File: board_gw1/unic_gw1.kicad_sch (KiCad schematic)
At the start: 109 parts, among them Q1 2N7002, Q10 2N7002, Q11 2N7002, Q12 2N7002, Q13 2N7002, Q14 2N7002, Q15 2N7002, Q16 2N7002, Q17 2N7002, Q18 2N7002, Q19 2N7002, Q2 2N7002, Q20 2N7002, Q21 2N7002, Q22 2N7002, Q23 2N7002, Q24 2N7002, Q25 2N7002, Q26 2N7002, Q27 2N7002, Q28 2N7002, Q29 2N7002, Q3 2N7002, Q30 2N7002, Q31 2N7002, Q32 2N7002, Q33 2N7002, Q34 2N7002, Q35 2N7002, Q36 2N7002, Q37 2N7002, Q38 2N7002, Q39 2N7002, Q4 2N7002, Q40 2N7002, Q5 2N7002, Q6 2N7002, Q7 2N7002, Q8 2N7002, Q9 2N7002, U1 GW1N-LV9QN88C6_I5_, U2 LM3480-3.3, U3 LM3480-5.0, U4 ESP-PSRAM32, U5 AT25SF081-XMHF-X, U6 AP62150Z6, X1 ASE-xxxMHz

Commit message: Added extra diodes to shunt ESD path.
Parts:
- added D21, D22, D23, D24, D25, D26, D27, D28, D29, D30: BAT54CV, Package_TO_SOT_SMD:SOT-666, symbol UNIC:BAT54CV
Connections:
- net +3V3: now also D21.3 (A), D21.3 (A), D21.6 (A), D21.6 (A), D22.3 (A), D22.3 (A), D22.6 (A), D22.6 (A), D23.3 (A), D23.3 (A), D23.6 (A), D23.6 (A), D24.3 (A), D24.3 (A), D24.6 (A), D24.6 (A), D25.3 (A), D25.3 (A), D25.6 (A), D25.6 (A), D26.3 (A), D26.3 (A), D26.6 (A), D26.6 (A), D27.3 (A), D27.3 (A), D27.6 (A), D27.6 (A), D28.3 (A), D28.3 (A), D28.6 (A), D28.6 (A), D29.3 (A), D29.3 (A), D29.6 (A), D29.6 (A), D30.3 (A), D30.3 (A), D30.6 (A), D30.6 (A)
- net PIN10_F: now also D23.2 (K)
- net PIN11_F: now also D23.4 (K)
- net PIN12_F: now also D23.5 (K)
- net PIN13_F: now also D24.1 (K)
- net PIN14_F: now also D24.2 (K)
- net PIN15_F: now also D24.4 (K)
- net PIN16_F: now also D24.5 (K)
- net PIN17_F: now also D25.1 (K)
- net PIN18_F: now also D25.2 (K)
- net PIN19_F: now also D25.4 (K)
- net PIN1_F: now also D21.1 (K)
- net PIN20_F: now also D25.5 (K)
- net PIN21_F: now also D26.1 (K)
- net PIN22_F: now also D26.2 (K)
- net PIN23_F: now also D26.4 (K)
- net PIN24_F: now also D26.5 (K)
- net PIN25_F: now also D27.1 (K)
- net PIN26_F: now also D27.2 (K)
- net PIN27_F: now also D27.4 (K)
- net PIN28_F: now also D27.5 (K)
- net PIN29_F: now also D28.1 (K)
- net PIN2_F: now also D21.2 (K)
- net PIN30_F: now also D28.2 (K)
- net PIN31_F: now also D28.4 (K)
- net PIN32_F: now also D28.5 (K)
- net PIN33_F: now also D29.1 (K)
- net PIN34_F: now also D29.2 (K)
- net PIN35_F: now also D29.4 (K)
- net PIN36_F: now also D29.5 (K)
- net PIN37_F: now also D30.1 (K)
- net PIN38_F: now also D30.2 (K)
- net PIN39_F: now also D30.4 (K)
- net PIN3_F: now also D21.4 (K)
- net PIN40_F: now also D30.5 (K)
- net PIN4_F: now also D21.5 (K)
- net PIN5_F: now also D22.1 (K)
- net PIN6_F: now also D22.2 (K)
- net PIN7_F: now also D22.4 (K)
- net PIN8_F: now also D22.5 (K)
- net PIN9_F: now also D23.1 (K)
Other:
- note added: "TODO: 3.3 needs to be a switcher! At 12V input power we can't sustain even 100mA I/O current. Static input current for an LS gate is 0.1mA. This gives us <10mA static output current. *THAT* We can sustain with an LDO See http://raven1.magix.net/Ti%20TTL%20DataBook%20vol1.pdf, page 20 https://ecelabs.njit.edu/fed101/resources/Motorola_Short_Version.pdf page 12 Detailed answer: https://electronics.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"
- note added: "There are dual- 7002 devices. https://assets.nexperia.com/documents/data-sheet/NX7002BKXB.pdf https://toshiba.semicon-storage.com/info/SSM6N7002BFE_datasheet_en_20140301.pdf?did=2282&prodName=SSM6N7002BFE https://www.diodes.com/assets/Datasheets/ds30639.pdf - has multiple sources All of these are cheaper than 2 single ones"
- moved on the sheet: C18, C20, C22, C23, D10A, D10B, D11A, D11B, D12A, D12B, D13A, D13B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

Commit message: GW1-based board is fully routed. Cleanup still needed!
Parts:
- removed D1, D10, D11, D12, D13, D14, D15, D16, D17, D18, D19, D2, D20, D3, D4, D5, D6, D7, D8, D9: BAT54SDW-7-F, UNIC:SOT65P210X110-6N, symbol UNIC:BAT54SDW-7-F
- removed J_EXT1: Conn_01x23_MountingPin, UNIC:Molex_502598-2393_2Rows-23Pins-1MP_P0.60mm_Horizontal, symbol Connector_Generic_MountingPin:Conn_01x23_MountingPin
- removed U3: LM3480-5.0, Package_TO_SOT_SMD:SOT-23, symbol Regulator_Linear:LM3480-5.0
- added D1, D11, D2, D3, D4, D5, D6, D7, D8, D9: BAT54DF, UNIC:SOT65P210X110-6N, symbol UNIC:BAT54DF
- added J_EXT1: Conn_01x27_MountingPin, UNIC:Molex_502598-2793_2Rows-23P~0.60mm_Horizontal, symbol Connector_Generic_MountingPin:Conn_01x27_MountingPin
- added R14: 4.99k, Resistor_SMD:R_0402_1005Metric_Pad0.72x0.64mm_HandSolder, symbol Device:R_Small_US
- added R15, R16: 10k, Resistor_SMD:R_0402_1005Metric_Pad0.72x0.64mm_HandSolder, symbol Device:R_Small_US
- added U3: AP2202K-ADJ, Package_TO_SOT_SMD:SOT-23-5, symbol Regulator_Linear:AP2204K-ADJ
- C3: value 0.1u -> 2.2u
- J_JTAG1: footprint Connector_PinHeader_1.27mm:PinHeader_2x06_P1.27mm_Vertical_SMD -> UNIC:PinHeader_2x06_P1.27mm_Vertical_SMD
- Q1, Q10, Q11, Q12, Q13, Q14, Q15, Q16, Q17, Q18, Q19, Q2, Q20, Q21, Q22, Q23, Q24, Q25, Q26, Q27, Q28, Q29, Q3, Q30, Q31, Q32, Q33, Q34, Q35, Q36, Q37, Q38, Q39, Q4, Q40, Q5, Q6, Q7, Q8, Q9: footprint Package_DFN_QFN:Diodes_DFN1006-3 -> UNIC:SOT-883
- R11, R3: value 1k -> 10k
- R12: value DNC -> 10k
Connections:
- net RECONIFG_N is gone; now on net RECONFIG_N: R7.2, U1.9 (IOL13B/RECONFIG_N)
- net SER_RXD is gone; now on net IO6B: J_JTAG1.1 (Pin_1)
- net SER_TXD is gone; now on net IO6A: J_JTAG1.2 (Pin_2)
- net +3V3: now also J_EXT1.25 (Pin_25), J_EXT1.26 (Pin_26), R16.1
- net +5V: now also J_EXT1.27 (Pin_27), R14.1, U3.5 (VOUT)
- net GND: now also D1.5, D1.5, D1.5, D1.5, D11.5, D11.5, D11.5, D11.5, D2.5, D2.5, D2.5, D2.5, D3.5, D3.5, D3.5, D3.5, D4.5, D4.5, D4.5, D4.5, D5.5, D5.5, D5.5, D5.5, D6.5, D6.5, D6.5, D6.5, D7.5, D7.5, D7.5, D7.5, D8.5, D8.5, D8.5, D8.5, D9.5, D9.5, D9.5, D9.5, J_EXT1.11 (Pin_11), J_EXT1.14 (Pin_14), J_EXT1.17 (Pin_17), J_EXT1.20 (Pin_20), J_EXT1.23 (Pin_23), J_EXT1.8 (Pin_8), J_EXT1.MP (MountPin), R15.2, U3.2 (GND)
- net IO1A: now also J_EXT1.7 (Pin_7)
- net IO1B: now also U1.38 (IOB31B), J_EXT1.9 (Pin_9); no longer U1.36 (IOB29B/GCLKC_4)
- net IO2A: now also U1.36 (IOB29B/GCLKC_4), J_EXT1.10 (Pin_10); no longer U1.35 (IOB29A/GCLKT_4)
- net IO2B: now also U1.35 (IOB29A/GCLKT_4), J_EXT1.12 (Pin_12); no longer U1.34 (IOB23B)
- net IO3A: now also U1.39 (IOB33A), J_EXT1.13 (Pin_13); no longer U1.33 (IOB23A)
- net IO3B: now also U1.40 (IOB33B), J_EXT1.15 (Pin_15); no longer U1.32 (IOB17B)
- net IO4A: now also J_EXT1.16 (Pin_16)
- net IO4B: now also U1.32 (IOB17B), J_EXT1.18 (Pin_18); no longer U1.30 (IOB13B)
- net IO5A: now also U1.41 (IOB41A), J_EXT1.19 (Pin_19); no longer U1.29 (IOB13A)
- net IO5B: now also U1.42 (IOB41B), J_EXT1.21 (Pin_21); no longer U1.28 (IOB11B)
- net IO6A: now also U1.33 (IOB23A), J_EXT1.22 (Pin_22); no longer U1.26 (IOB8B)
- net IO6B: now also U1.34 (IOB23B), J_EXT1.24 (Pin_24); no longer U1.25 (IOB8A)
- net JTAG_SEL_N: now also J_EXT1.1 (Pin_1), R16.2
- net JTAG_TCK: now also J_EXT1.6 (Pin_6)
- net JTAG_TDI: now also J_JTAG1.10 (Pin_10), J_EXT1.2 (Pin_2)
- net JTAG_TDO: now also J_EXT1.4 (Pin_4); no longer J_JTAG1.10 (Pin_10)
- net JTAG_TMS: now also J_EXT1.5 (Pin_5)
- net LCD_CS_N: now also U1.79 (IOT12B); no longer U1.54 (IOR15A/DIN/CLKHOLD_N)
- net LCD_RST_N: now also R2.2, R3.1, U1.87 (IOT6B/MODE1); no longer U1.53 (IOR15B/DOUT/WE_N)
- net LINE: now also D1.2, D1.2, D1.2, D1.2, D11.2, D11.2, D11.2, D11.2, D2.2, D2.2, D2.2, D2.2, D3.2, D3.2, D3.2, D3.2, D4.2, D4.2, D4.2, D4.2, D5.2, D5.2, D5.2, D5.2, D6.2, D6.2, D6.2, D6.2, D7.2, D7.2, D7.2, D7.2, D8.2, D8.2, D8.2, D8.2, D9.2, D9.2, D9.2, D9.2, U3.1 (VIN), U3.3 (EN)
- net PIN1: now also D1.1
- net PIN10: now also D3.3
- net PIN10_F: now also U1.69 (IOT42A); no longer U1.51 (IOR17B/GCLKC_3)
- net PIN11: now also Q19.3 (D), D5.1; no longer Q11.3 (D)
- net PIN11_F: now also D25.1 (K), Q19.2 (S), U1.73 (IOT39A); no longer D23.4 (K), Q11.2 (S), U1.63 (IOR5A/RPLL_T_IN)
- net PIN12: now also Q15.3 (D), D4.1; no longer Q12.3 (D)
- net PIN12_F: now also D24.1 (K), Q15.2 (S), U1.50 (IOR22B); no longer D23.5 (K), Q12.2 (S), U1.68 (IOT42B)
- net PIN13: now also Q20.3 (D), D5.3; no longer Q13.3 (D)
- net PIN13_F: now also D25.2 (K), Q20.2 (S), U1.72 (IOT39B); no longer D24.1 (K), Q13.2 (S), U1.69 (IOT42A)
- net PIN14: now also D3.6
- net PIN14_F: now also D23.5 (K), U1.63 (IOR5A/RPLL_T_IN); no longer D24.2 (K), U1.70 (IOT41B)
- net PIN15: now also Q13.3 (D), D3.4; no longer Q15.3 (D)
- net PIN15_F: now also D23.4 (K), Q13.2 (S), U1.68 (IOT42B); no longer D24.4 (K), Q15.2 (S), U1.71 (IOT41A)
- net PIN16: now also Q18.3 (D), D4.6; no longer Q16.3 (D)
- net PIN16_F: now also Q18.2 (S), U1.54 (IOR15A/DIN/CLKHOLD_N); no longer Q16.2 (S), U1.72 (IOT39B)
- net PIN17: now also D4.4
- net PIN17_F: now also D24.4 (K), U1.53 (IOR15B/DOUT/WE_N); no longer D25.1 (K), U1.73 (IOT39A)
- net PIN18: now also Q16.3 (D), D4.3; no longer Q18.3 (D)
- net PIN18_F: now also D24.2 (K), Q16.2 (S), U1.51 (IOR17B/GCLKC_3); no longer D25.2 (K), Q18.2 (S), U1.74 (IOT38B)
- net PIN19: now also Q22.3 (D), D5.6; no longer Q19.3 (D)
- net PIN19_F: now also D25.5 (K), Q22.2 (S), U1.49 (IOR24A); no longer D25.4 (K), Q19.2 (S), U1.75 (IOT38A)
- net PIN1_F: now also U1.29 (IOB13A); no longer U1.38 (IOB31B)
- net PIN2: now also Q4.3 (D), D1.6; no longer Q2.3 (D)
- net PIN20: now also Q21.3 (D), D5.4; no longer Q20.3 (D)
- net PIN20_F: now also D25.4 (K), Q21.2 (S), U1.71 (IOT41A); no longer D25.5 (K), Q20.2 (S), U1.76 (IOT37B)
- net PIN21: now also Q12.3 (D), D11.3; no longer Q21.3 (D)
- net PIN21_F: now also D26.2 (K), Q12.2 (S), U1.75 (IOT38A); no longer D26.1 (K), Q21.2 (S), U1.77 (IOT37A)
- net PIN22: now also Q11.3 (D), D11.1; no longer Q22.3 (D)
- net PIN22_F: now also D26.1 (K), Q11.2 (S), U1.77 (IOT37A); no longer D26.2 (K), Q22.2 (S), U1.79 (IOT12B)
- net PIN23: now also Q27.3 (D), D6.4; no longer Q23.3 (D)
- net PIN23_F: now also D27.4 (K), Q27.2 (S); no longer D26.4 (K), Q23.2 (S)
- net PIN24: now also D6.3
- net PIN24_F: now also D27.2 (K), U1.82 (IOT11A); no longer D26.5 (K), U1.81 (IOT11B)
- net PIN25: now also Q23.3 (D), D6.1; no longer Q25.3 (D)
- net PIN25_F: now also Q23.2 (S), U1.83 (IOT10B); no longer Q25.2 (S), U1.82 (IOT11A)
- net PIN26: now also Q31.3 (D), D7.4; no longer Q26.3 (D)
- net PIN26_F: now also D28.4 (K), Q31.2 (S), U1.85 (IOT8B); no longer D27.2 (K), Q26.2 (S), U1.83 (IOT10B)
- net PIN27: now also Q29.3 (D), D7.1; no longer Q27.3 (D)
- net PIN27_F: now also D28.1 (K), Q29.2 (S), U1.3 (IOL2A); no longer D27.4 (K), Q27.2 (S), U1.84 (IOT10A)
- net PIN28: now also Q25.3 (D), D11.4; no longer Q28.3 (D)
- net PIN28_F: now also D26.4 (K), Q25.2 (S), U1.11 (IOL15A/GCLKT_6); no longer D27.5 (K), Q28.2 (S), U1.85 (IOT8B)
- net PIN29: now also Q28.3 (D), D6.6; no longer Q29.3 (D)
- net PIN29_F: now also D27.5 (K), Q28.2 (S), U1.81 (IOT11B); no longer D28.1 (K), Q29.2 (S), U1.86 (IOT8A)
- net PIN2_F: now also D21.5 (K), Q4.2 (S), U1.30 (IOB13B); no longer D21.2 (K), Q2.2 (S), U1.39 (IOB33A)
- net PIN3: now also D1.4
- net PIN30: now also Q26.3 (D), D11.6; no longer Q30.3 (D)
- net PIN30_F: now also D26.5 (K), Q26.2 (S), U1.74 (IOT38B); no longer D28.2 (K), Q30.2 (S), U1.3 (IOL2A)
- net PIN31: now also Q30.3 (D), D7.3; no longer Q31.3 (D)
- net PIN31_F: now also D28.2 (K), Q30.2 (S), U1.86 (IOT8A); no longer D28.4 (K), Q31.2 (S), U1.15 (IOL26A)
- net PIN32: now also D7.6
- net PIN32_F: now also U1.84 (IOT10A); no longer U1.14 (IOL22B)
- net PIN33: now also Q36.3 (D), D8.6; no longer Q33.3 (D)
- net PIN33_F: now also D29.5 (K), Q36.2 (S); no longer D29.1 (K), Q33.2 (S)
- net PIN34: now also Q35.3 (D), D8.4; no longer Q34.3 (D)
- net PIN34_F: now also D29.4 (K), Q35.2 (S), U1.14 (IOL22B); no longer D29.2 (K), Q34.2 (S), U1.11 (IOL15A/GCLKT_6)
- net PIN35: now also Q34.3 (D), D8.3; no longer Q35.3 (D)
- net PIN35_F: now also D29.2 (K), Q34.2 (S), U1.15 (IOL26A); no longer D29.4 (K), Q35.2 (S), U1.16 (IOL26B)
- net PIN36: now also Q33.3 (D), D8.1; no longer Q36.3 (D)
- net PIN36_F: now also D29.1 (K), Q33.2 (S), U1.16 (IOL26B); no longer D29.5 (K), Q36.2 (S), U1.17 (IOB2A)
- net PIN37: now also Q39.3 (D), D9.4; no longer Q37.3 (D)
- net PIN37_F: now also D30.4 (K), Q39.2 (S), U1.20 (IOB4B); no longer D30.1 (K), Q37.2 (S), U1.18 (IOB2B)
- net PIN38: now also D9.3
- net PIN38_F: now also U1.18 (IOB2B); no longer U1.19 (IOB4A)
- net PIN39: now also Q37.3 (D), D9.1; no longer Q39.3 (D)
- net PIN39_F: now also D30.1 (K), Q37.2 (S), U1.17 (IOB2A); no longer D30.4 (K), Q39.2 (S), U1.20 (IOB4B)
- net PIN3_F: now also U1.27 (IOB11A); no longer U1.40 (IOB33B)
- net PIN4: now also Q2.3 (D), D1.3; no longer Q4.3 (D)
- net PIN40: now also D9.6
- net PIN40_F: now also U1.19 (IOB4A); no longer U1.27 (IOB11A)
- net PIN4_F: now also D21.2 (K), Q2.2 (S), U1.28 (IOB11B); no longer D21.5 (K), Q4.2 (S), U1.41 (IOB41A)
- net PIN5: now also Q8.3 (D), D2.6; no longer Q5.3 (D)
- net PIN5_F: now also D22.5 (K), Q8.2 (S), U1.26 (IOB8B); no longer D22.1 (K), Q5.2 (S), U1.42 (IOB41B)
- net PIN6: now also Q7.3 (D), D2.4; no longer Q6.3 (D)
- net PIN6_F: now also D22.4 (K), Q7.2 (S), U1.25 (IOB8A); no longer D22.2 (K), Q6.2 (S), U1.47 (IOB43B)
- net PIN7: now also Q6.3 (D), D2.3; no longer Q7.3 (D)
- net PIN7_F: now also D22.2 (K), Q6.2 (S), U1.47 (IOB43B); no longer D22.4 (K), Q7.2 (S), U1.48 (IOR24B)
- net PIN8: now also Q5.3 (D), D2.1; no longer Q8.3 (D)
- net PIN8_F: now also D22.1 (K), Q5.2 (S), U1.48 (IOR24B); no longer D22.5 (K), Q8.2 (S), U1.49 (IOR24A)
- net PIN9: now also D3.1
- net PIN9_F: now also U1.70 (IOT41B); no longer U1.50 (IOR22B)
- net PSRAM_CS_N: now also U1.76 (IOT37B); no longer R12.1, U1.57 (IOR13A/FASTRD_N/D3)
- net RECONFIG_N: now also J_EXT1.3 (Pin_3)
- net JTAG_RST: no longer names the net of J_JTAG1.12 (Pin_12)
- new net: R12.1, U1.57 (IOR13A/FASTRD_N/D3)
- new net: R14.2, R15.1, U3.4 (ADJ)
- no-connect marks 2 -> 3
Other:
- note added: "5V is trimmed to 4.5V"
- note added: "Molex connector: https://www.molex.com/en-us/products/part-detail/502598-2793 Mating cable: 15015-xx27 Corresponding flexes: https://rhu004.sma-promail.com/SQLImages/kelmscott/Molex/PDF_Images/987650-6721.PDF 0.3A per contact for the connector, 0.2A for the cable"
- note added: "There are a ton of TVS diodes of this persuation: https://assets.nexperia.com/documents/data-sheet/IP4221CZ6-XS.pdf They are great, cheap, but can't stand more than 5V. They also have a 0.7V forward voltage. Another single-source solution: http://www.smc-diodes.com/propdf/BAT54DF%20N2313%20REV.-.pdf This is 4 pairs of diodes in one package. Not replacing as current option with several second sour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"
- note added: "There are dual- 7002 devices. https://assets.nexperia.com/documents/data-sheet/NX7002BKXB.pdf https://toshiba.semicon-storage.com/info/SSM6N7002BFE_datasheet_en_20140301.pdf?did=2282&prodName=SSM6N7002BFE https://www.diodes.com/assets/Datasheets/ds30639.pdf - has multiple sources Single ones: NX7002BKH or NX7002BKM"
- note removed: "Molex connector: https://www.molex.com/en-us/products/part-detail/502598-2393 Mating cable: 15015-xx23 Corresponding flexes: https://rhu004.sma-promail.com/SQLImages/kelmscott/Molex/PDF_Images/987650-6721.PDF 0.3A per contact for the connector, 0.2A for the cable"
- note removed: "There are dual- 7002 devices. https://assets.nexperia.com/documents/data-sheet/NX7002BKXB.pdf https://toshiba.semicon-storage.com/info/SSM6N7002BFE_datasheet_en_20140301.pdf?did=2282&prodName=SSM6N7002BFE https://www.diodes.com/assets/Datasheets/ds30639.pdf - has multiple sources All of these are cheaper than 2 single ones"
- moved on the sheet: C3, U1

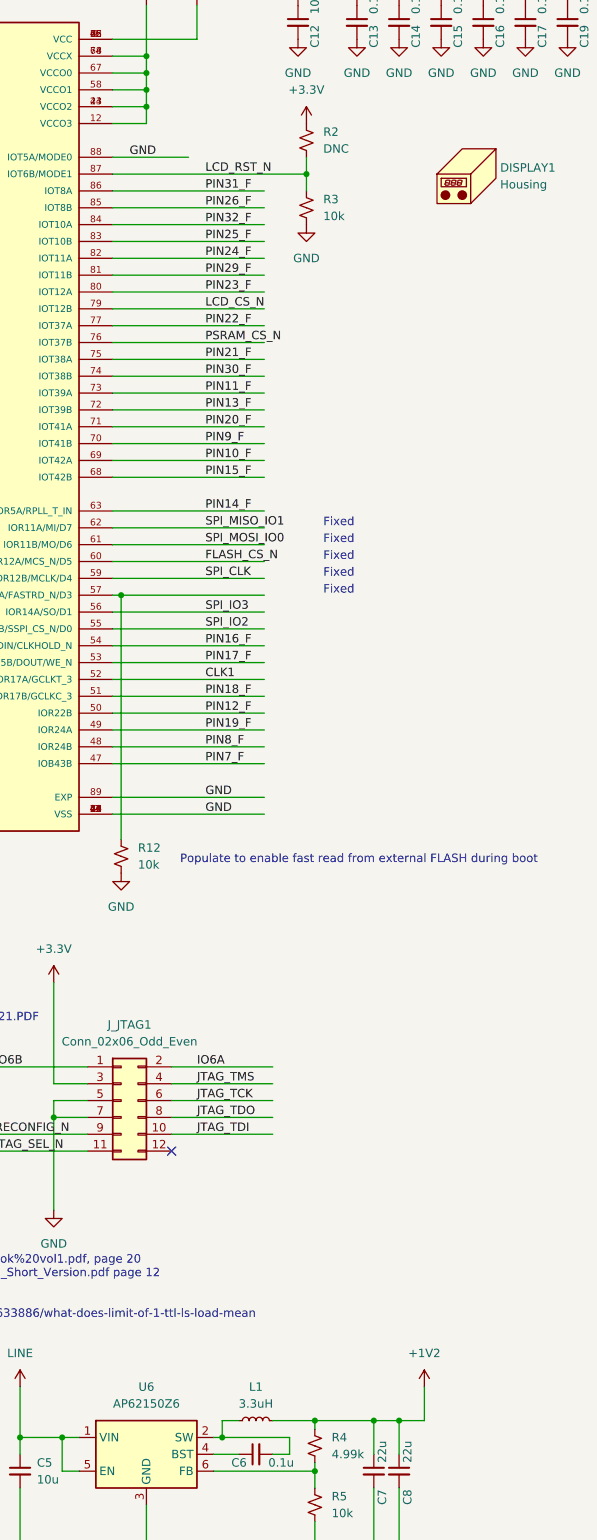
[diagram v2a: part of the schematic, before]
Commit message: Migrated to KiCad 7.
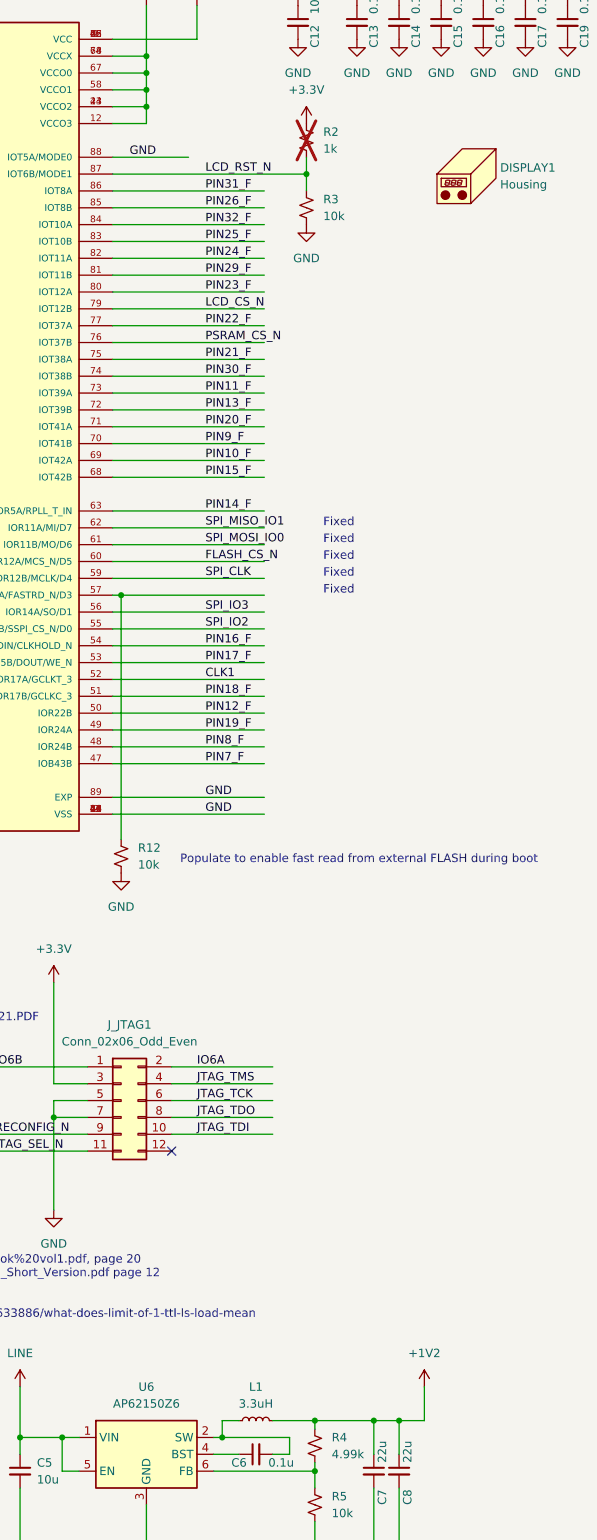
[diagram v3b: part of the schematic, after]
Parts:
- R2: value DNC -> 1k; now not fitted

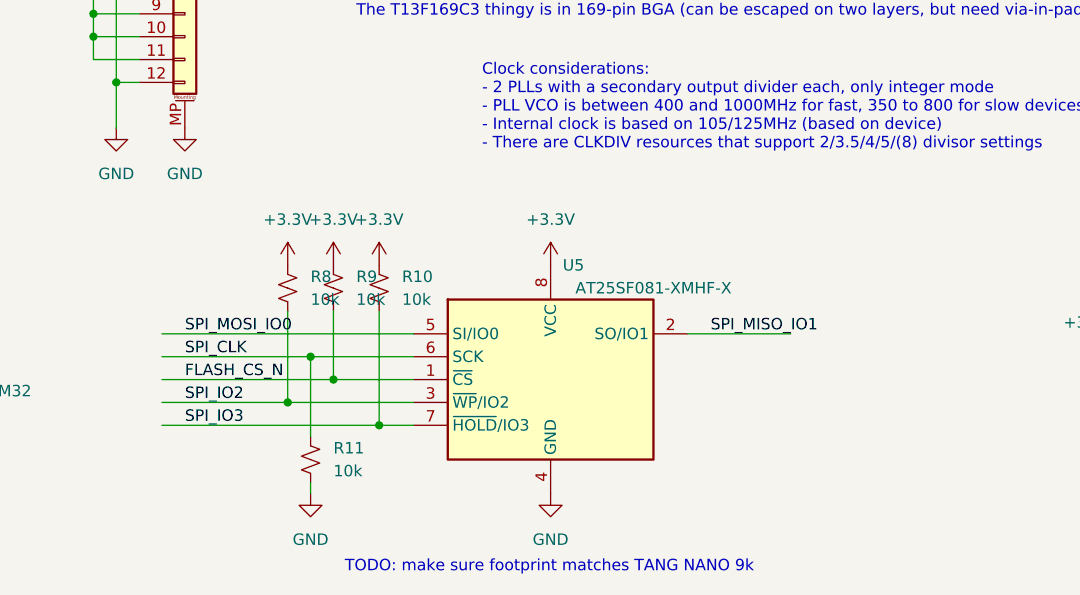
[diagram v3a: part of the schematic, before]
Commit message: Updated FLASH part to package that's actually available.
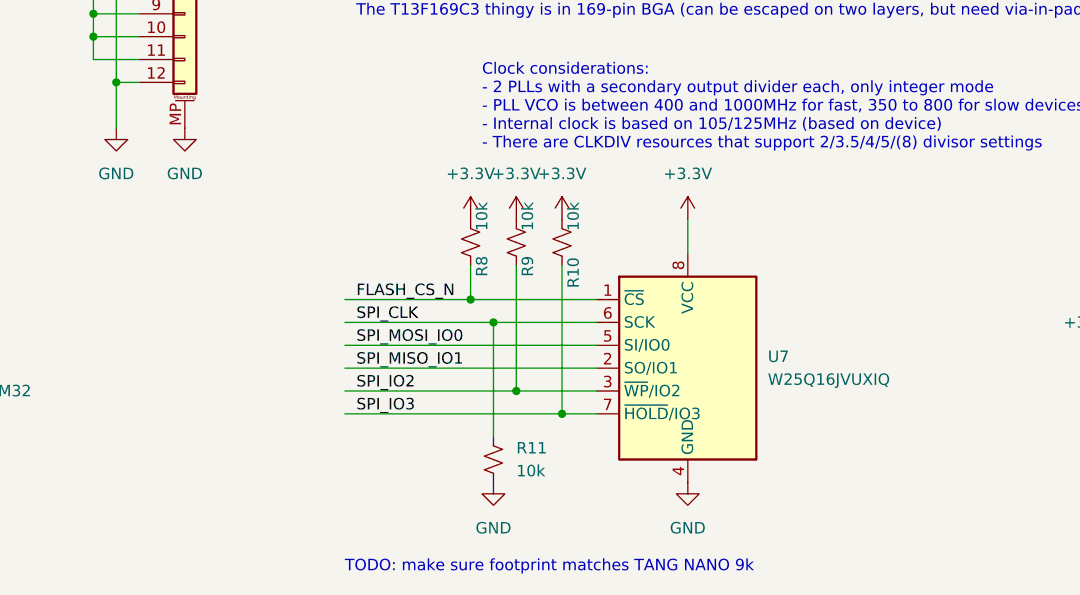
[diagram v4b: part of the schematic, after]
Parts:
- removed U5: AT25SF081-XMHF-X, Package_SO:TSSOP-8_4.4x3mm_P0.65mm, symbol Memory_Flash:AT25SF081-XMHF-X
- added U7: W25Q16JVUXIQ, UNIC:W25Q16JVUXIQ_TR, symbol UNIC:W25Q16JVUXIQ
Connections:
- net +3V3: now also U7.8 (VCC)
- net FLASH_CS_N: now also R8.2, U7.1 (~{CS}); no longer R9.2
- net GND: now also U7.4 (GND)
- net SPI_CLK: now also U7.6 (SCK)
- net SPI_IO2: now also R9.2, U7.3 (~{WP}/IO2); no longer R8.2
- net SPI_IO3: now also U7.7 (~{HOLD}/IO3)
- net SPI_MISO_IO1: now also U7.2 (SO/IO1)
- net SPI_MOSI_IO0: now also U7.5 (SI/IO0)

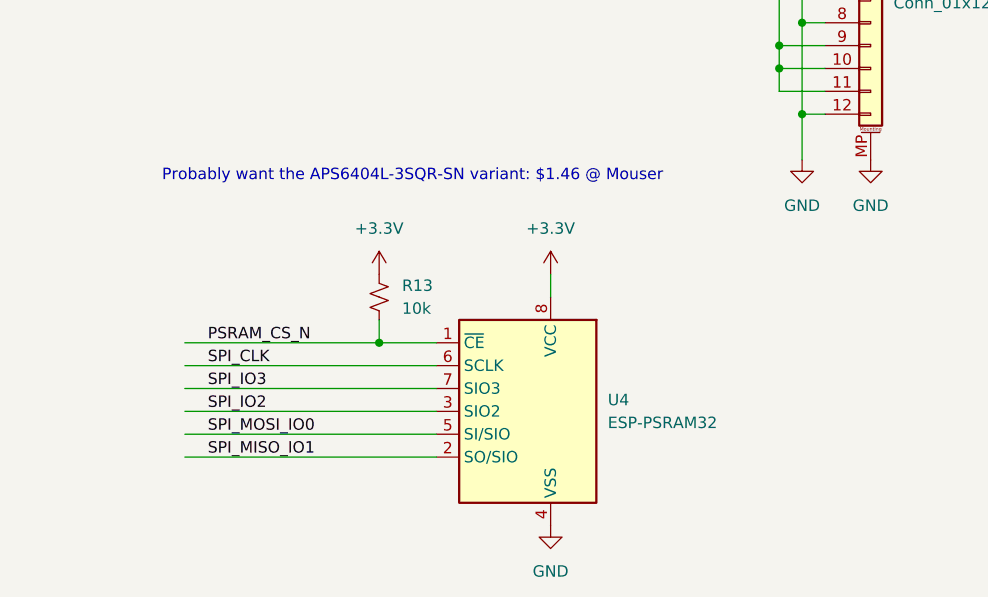
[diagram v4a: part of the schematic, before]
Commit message: Updated footprints for LCD connector and PSRAM
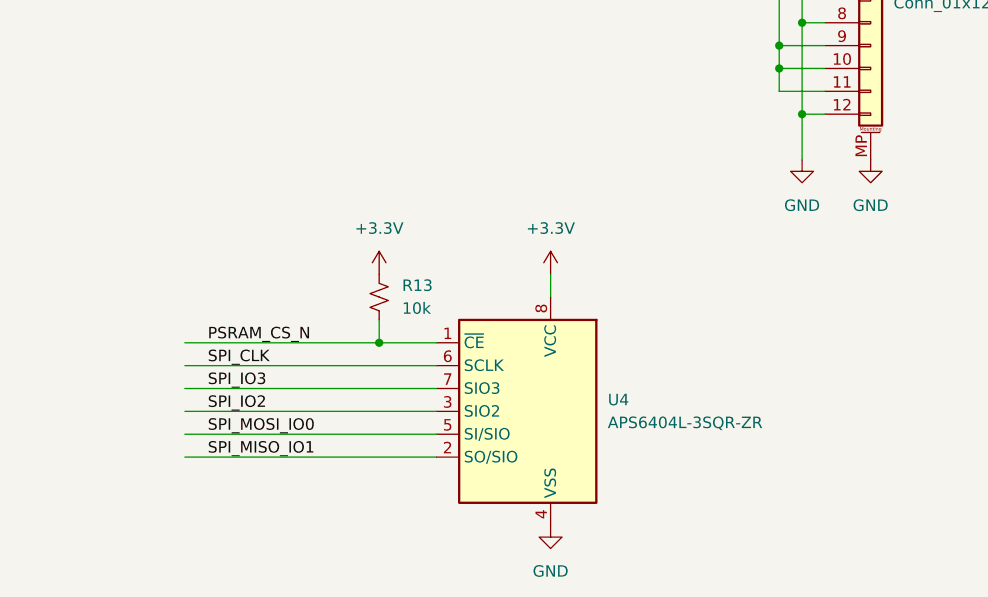
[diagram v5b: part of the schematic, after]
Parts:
- J_DISPLAY1: footprint UNIC:CF31121D0R0-05-NH -> UNIC:HRS_FH19C-12S-0.5SH_05_
- U4: value ESP-PSRAM32 -> APS6404L-3SQR-ZR; footprint Package_SO:SOIC-8_3.9x4.9mm_P1.27mm -> UNIC:W25Q16JVUXIQ_TR
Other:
- note removed: "Probably want the APS6404L-3SQR-SN variant: $1.46 @ Mouser"
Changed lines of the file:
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@@
     (effects (font (size 1.27 1.27)) (justify left bottom))
   )
-  (text "Probably want the APS6404L-3SQR-SN variant: $1.46 @ Mouser"
-    (at 77.47 358.14 0)
-    (effects (font (size 1.27 1.27)) (justify left bottom))
-  )
   (text "Dedicated pin" (at 105.41 83.82 0)
     (effects (font (size 1.27 1.27)) (justify right bottom))
@@
       (effects (font (size 1.27 1.27)) (justify left))
     )
-    (property "Footprint" "UNIC:CF31121D0R0-05-NH" (at 156.21 335.28 0)
+    (property "Footprint" "UNIC:HRS_FH19C-12S-0.5SH_05_" (at 156.21 335.28 0)
       (effects (font (size 1.27 1.27)) hide)
     )
@@
       (effects (font (size 1.27 1.27)) (justify right))
     )
-    (property "Value" "ESP-PSRAM32" (at 127 384.8099 0)
+    (property "Value" "APS6404L-3SQR-ZR" (at 127 384.8099 0)
       (effects (font (size 1.27 1.27)) (justify right))
     )
-    (property "Footprint" "Package_SO:SOIC-8_3.9x4.9mm_P1.27mm" (at 118.11 398.78 0)
+    (property "Footprint" "UNIC:W25Q16JVUXIQ_TR" (at 118.11 398.78 0)
       (effects (font (size 1.27 1.27)) hide)
     )
-    (property "Datasheet" "https://www.espressif.com/sites/default/files/documentation/esp-psram32_datasheet_en.pdf" (at 128.27 370.84 0)
+    (property "Datasheet" "https://www.mouser.com/datasheet/2/1127/APM_PSRAM_QSPI_APS6404L_3SQR_v2_3_PKG-1954826.pdf" (at 128.27 370.84 0)
       (effects (font (size 1.27 1.27)) hide)
     )
